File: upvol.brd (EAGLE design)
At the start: 30.8 x 20.2 mm, 11 parts, among them IC1 LM393D, J1 61300311121, J2 61300211121

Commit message: add
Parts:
- removed J2: 61300211121, Headers:61300211121
- added T1: s9014, transistor:SOT23-EBC
- R1, R2, R4: device OPL_Resistor:PR-D2.3XL6.5MM -> 52101-101-REV-A_v16:RC-MASTER-SMD_R0603MP
- R3: value 100 -> 4.7k; device OPL_Resistor:PR-D2.3XL6.5MM -> 52101-101-REV-A_v16:RC-MASTER-SMD_R0603MP
- moved J1 48.7 mm to (53.1, 5.93), turned to 90 degrees
- moved R2 40.4 mm to (55.3, 5.64), flipped to the bottom, turned to 90 degrees
- moved IC1 18.8 mm to (30.2, 4.37), turned to 270 degrees
- moved U$1 16.3 mm to (30.3, 6.85)
- moved C1 16.2 mm to (19.8, 6.63), turned to 270 degrees
- moved LED1 11.4 mm to (15.9, 3.43), turned to 270 degrees
- moved R1 8.29 mm to (25.3, 2.48), flipped to the bottom, turned to 90 degrees
- moved R3 6.56 mm to (25.8, 6.97), flipped to the bottom
- moved R5 5.38 mm to (8.90, 5.18)
- moved R4 5.33 mm to (21.6, 1.79), flipped to the bottom
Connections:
- new net N$5: IC1.1, T1.B
- net N$1: now also C1.2, U$1.C; no longer C1.1, U$1.E
- net OUT: now also T1.C; no longer IC1.1
- net V+: no longer J2.2
- net V-: now also C1.1, T1.E, U$1.E; no longer C1.2, J2.1, U$1.C
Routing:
- net V-: track 41.4 -> 66.4 mm
- net N$1: track 40.5 -> 16.1 mm, vias 1 -> 0
- net OUT: track 21.7 -> 43.1 mm
- net N$5: track 0.00 -> 15.7 mm
- net N$4: track 9.60 -> 22.6 mm, vias 0 -> 1
- net N$2: track 4.89 -> 11.5 mm
- net V+: track 52.7 -> 57.7 mm
- net N$3: track 4.02 -> 5.08 mm
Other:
- board size 30.8 x 20.2 mm -> 60.2 x 10.2 mm

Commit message: add
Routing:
- net V-: track 66.4 -> 77.7 mm, vias 0 -> 1
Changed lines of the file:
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@@
 <drawing>
 <settings>
-<setting alwaysvectorfont="yes"/>
+<setting alwaysvectorfont="no"/>
 <setting verticaltext="up"/>
 </settings>
@@
 <wire x1="19.812190625" y1="7.89995" x2="22.1752375" y2="7.89995" width="0.508" layer="16"/>
 <wire x1="22.1752375" y1="7.89995" x2="22.776696875" y2="8.501409375" width="0.508" layer="16" curve="90"/>
-<wire x1="32.758565625" y1="2.465203125" x2="46.8100875" y2="2.465203125" width="0.508" layer="16"/>
+<wire x1="32.758565625" y1="2.465203125" x2="43.5" y2="2.465203125" width="0.508" layer="16"/>
+<wire x1="43.5" y1="2.465203125" x2="46.8100875" y2="2.465203125" width="0.508" layer="16"/>
 <wire x1="46.8100875" y1="2.465203125" x2="46.83289375" y2="2.488009375" width="0.508" layer="16" curve="90"/>
 <wire x1="34.99303125" y1="7.334075" x2="37.000696875" y2="5.326409375" width="0.508" layer="1" curve="-90"/>
 <wire x1="22.776696875" y1="8.501409375" x2="23.94403125" y2="7.334075" width="0.508" layer="1" curve="90"/>
-<wire x1="53.135478125" y1="5.9283" x2="47.91481875" y2="5.9283" width="0.508" layer="16"/>
-<wire x1="47.91481875" y1="5.9283" x2="37.6025875" y2="5.9283" width="0.508" layer="16"/>
+<wire x1="53.135478125" y1="5.9283" x2="37.6025875" y2="5.9283" width="0.508" layer="16"/>
 <wire x1="37.6025875" y1="5.9283" x2="37.000696875" y2="5.326409375" width="0.508" layer="16" curve="90"/>
 <wire x1="19.7709625" y1="7.858721875" x2="19.812190625" y2="7.89995" width="0.508" layer="16" curve="90"/>
 <wire x1="23.94403125" y1="7.334075" x2="34.99303125" y2="7.334075" width="0.508" layer="1"/>
-<wire x1="46.83289375" y1="2.488009375" x2="47.91481875" y2="3.569934375" width="0.3048" layer="16" curve="90"/>
-<wire x1="47.91481875" y1="3.569934375" x2="47.91481875" y2="5.9283" width="0.3048" layer="16"/>
-<wire x1="8.90229375" y1="2.64291875" x2="10.963003125" y2="2.64291875" width="0.3048" layer="16"/>
-<wire x1="10.963003125" y1="2.64291875" x2="13.4014125" y2="5.081328125" width="0.3048" layer="16" curve="90"/>
-<wire x1="13.4014125" y1="5.081328125" x2="13.4014125" y2="5.35995" width="0.3048" layer="16"/>
-<wire x1="13.4014125" y1="5.35995" x2="15.9414125" y2="7.89995" width="0.3048" layer="16" curve="-90"/>
-<wire x1="15.9414125" y1="7.89995" x2="19.812190625" y2="7.89995" width="0.3048" layer="16"/>
+<wire x1="53.135478125" y1="5.9283" x2="46.04" y2="5.9283" width="0.508" layer="1"/>
+<wire x1="46.04" y1="5.9283" x2="43.5" y2="3.3883" width="0.508" layer="1" curve="90"/>
+<wire x1="43.5" y1="3.3883" x2="43.5" y2="2.465203125" width="0.508" layer="1"/>
+<via x="43.5" y="2.465203125" extent="1-16" drill="0.35"/>
+<wire x1="8.90229375" y1="2.64291875" x2="10.888615625" y2="2.64291875" width="0.8128" layer="16"/>
+<wire x1="10.888615625" y1="2.64291875" x2="13.428615625" y2="5.18291875" width="0.8128" layer="16" curve="90"/>
+<wire x1="13.428615625" y1="6.0247375" x2="15.968615625" y2="8.5647375" width="0.8128" layer="16" curve="-90"/>
+<wire x1="22.71336875" y1="8.5647375" x2="22.776696875" y2="8.501409375" width="0.8128" layer="16" curve="-90"/>
+<wire x1="13.428615625" y1="5.18291875" x2="13.428615625" y2="6.0247375" width="0.8128" layer="16"/>
+<wire x1="15.968615625" y1="8.5647375" x2="22.71336875" y2="8.5647375" width="0.8128" layer="16"/>
 </signal>
 <signal name="N$1">

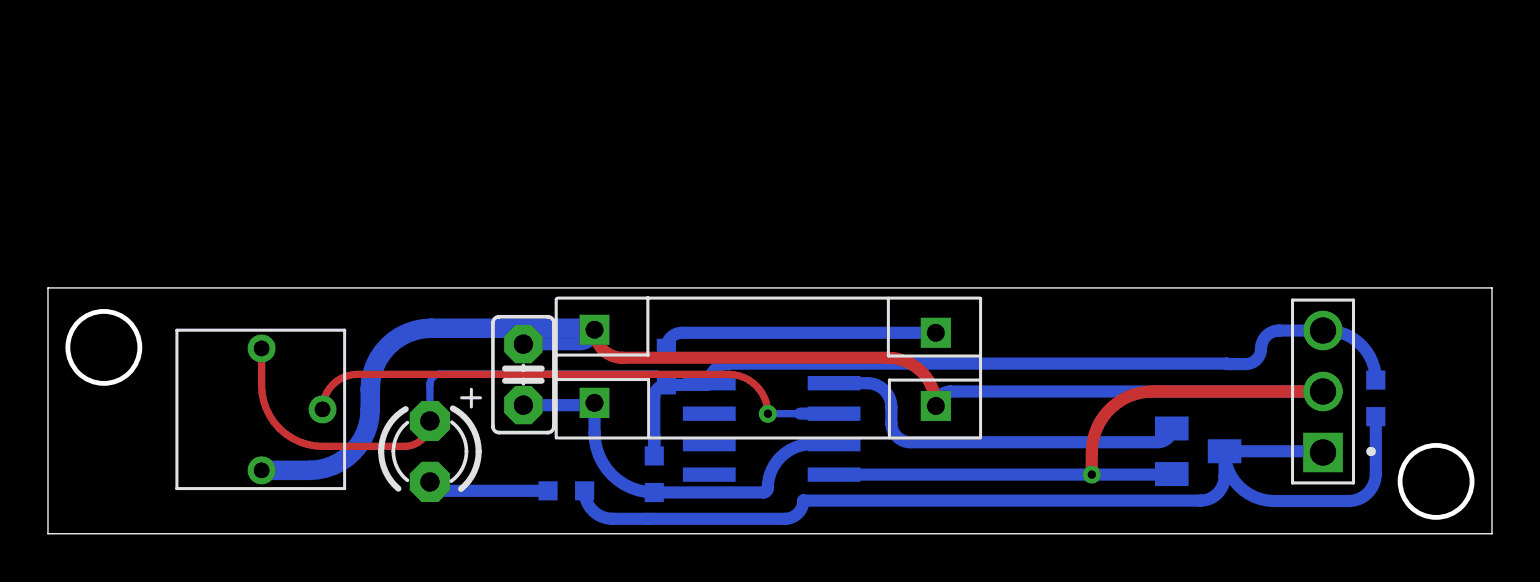
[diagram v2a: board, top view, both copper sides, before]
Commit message: 更新输入模块
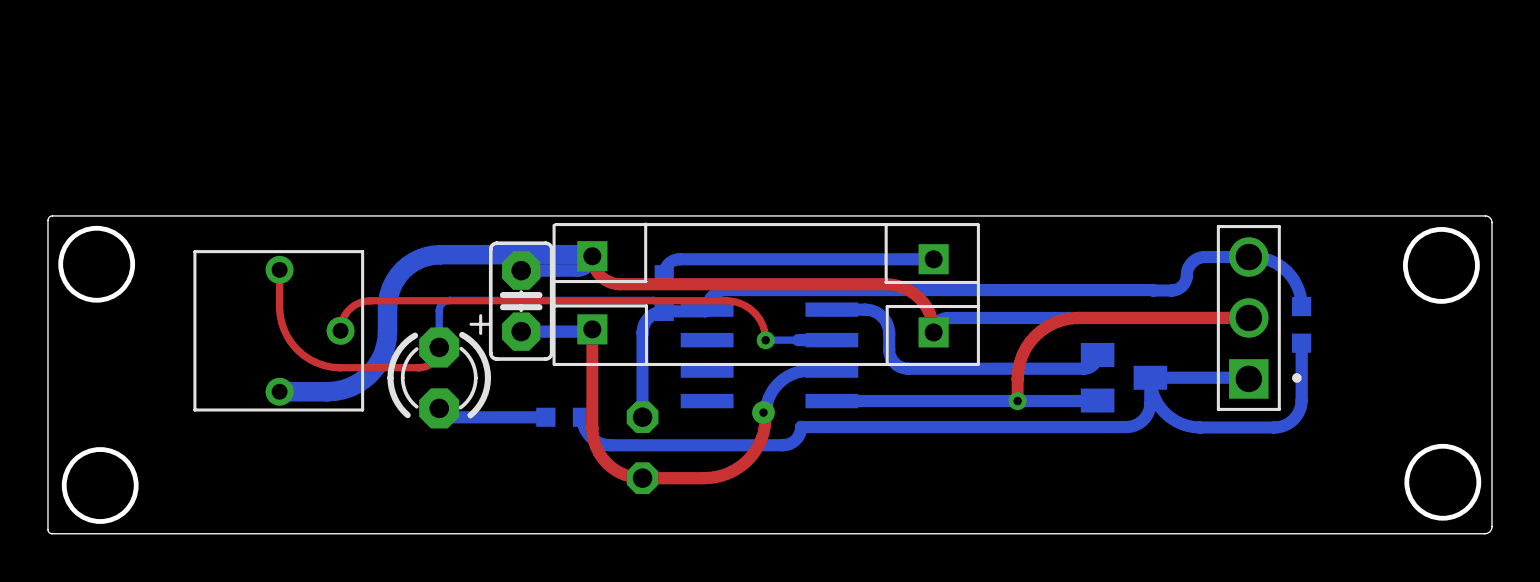
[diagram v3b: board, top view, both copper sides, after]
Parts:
- R1: device 52101-101-REV-A_v16:RC-MASTER-SMD_R0603MP -> rcl:0204V
- moved J1 4.35 mm to (50.0, 8.99)
- moved R2 4.35 mm to (52.2, 8.71)
- moved T1 4.35 mm to (44.8, 6.50)
- moved R5 3.36 mm to (9.65, 8.46)
- moved LED1 3.09 mm to (16.3, 6.49)
- moved C1 3.07 mm to (19.7, 9.69)
- moved IC1 3.07 mm to (30.1, 7.43)
- moved R3 3.07 mm to (25.7, 10.0)
- moved R4 3.07 mm to (21.5, 4.85)
- moved U$1 3.07 mm to (30.2, 9.91)
- moved R1 1.21 mm to (24.8, 3.59)
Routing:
- net V-: track 77.7 -> 70.9 mm
- net N$1: track 16.1 -> 20.0 mm, vias 0 -> 1
- net OUT: track 43.1 -> 40.1 mm
- net N$5: track 15.7 -> 12.7 mm
- net V+: track 57.7 -> 54.9 mm
- net N$4: track 22.6 -> 21.7 mm
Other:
- board size 60.2 x 10.2 mm -> 60.2 x 13.2 mm
